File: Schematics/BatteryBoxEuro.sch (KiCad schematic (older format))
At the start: 16 parts, among them K1 JD2912-1Z-12VDC_40A, P1 Conn_WallPlug, U1 Terminal16, U2 F_Distributor, U3 NAC3MPA-1-WOT, U4 DPlusSimulator, U5 Pulser, U6 230V_KfzCharger, X1 X3, X2 12VKfz_Plug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

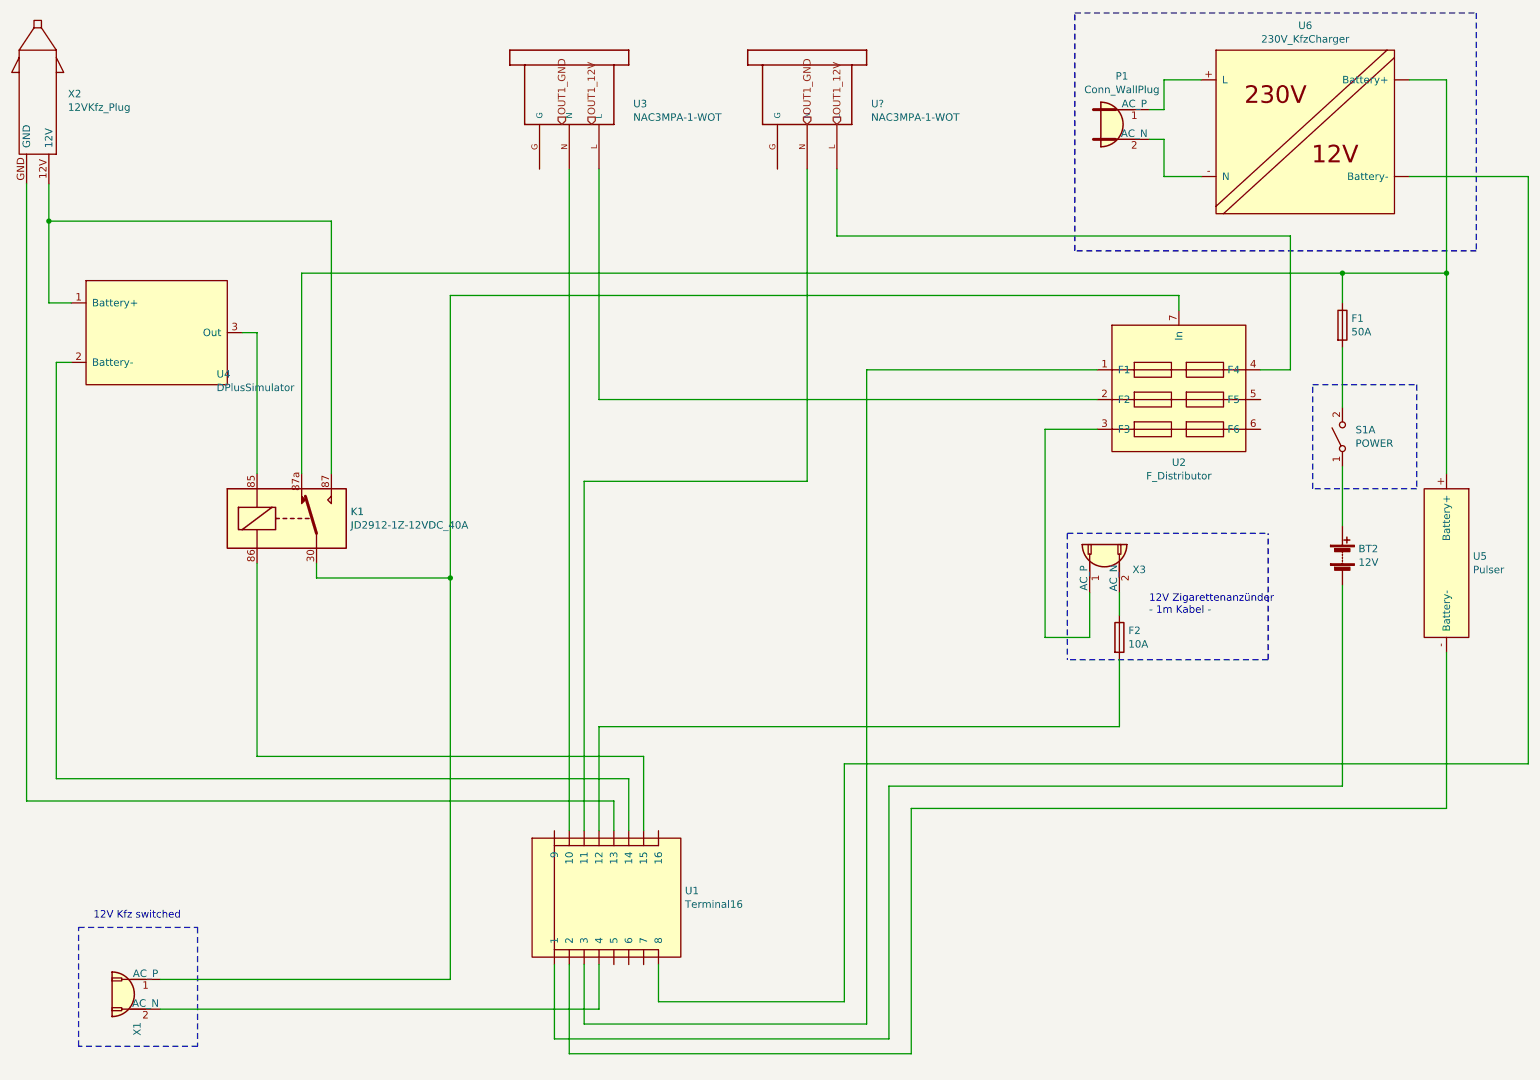
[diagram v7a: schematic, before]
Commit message: optimize layout
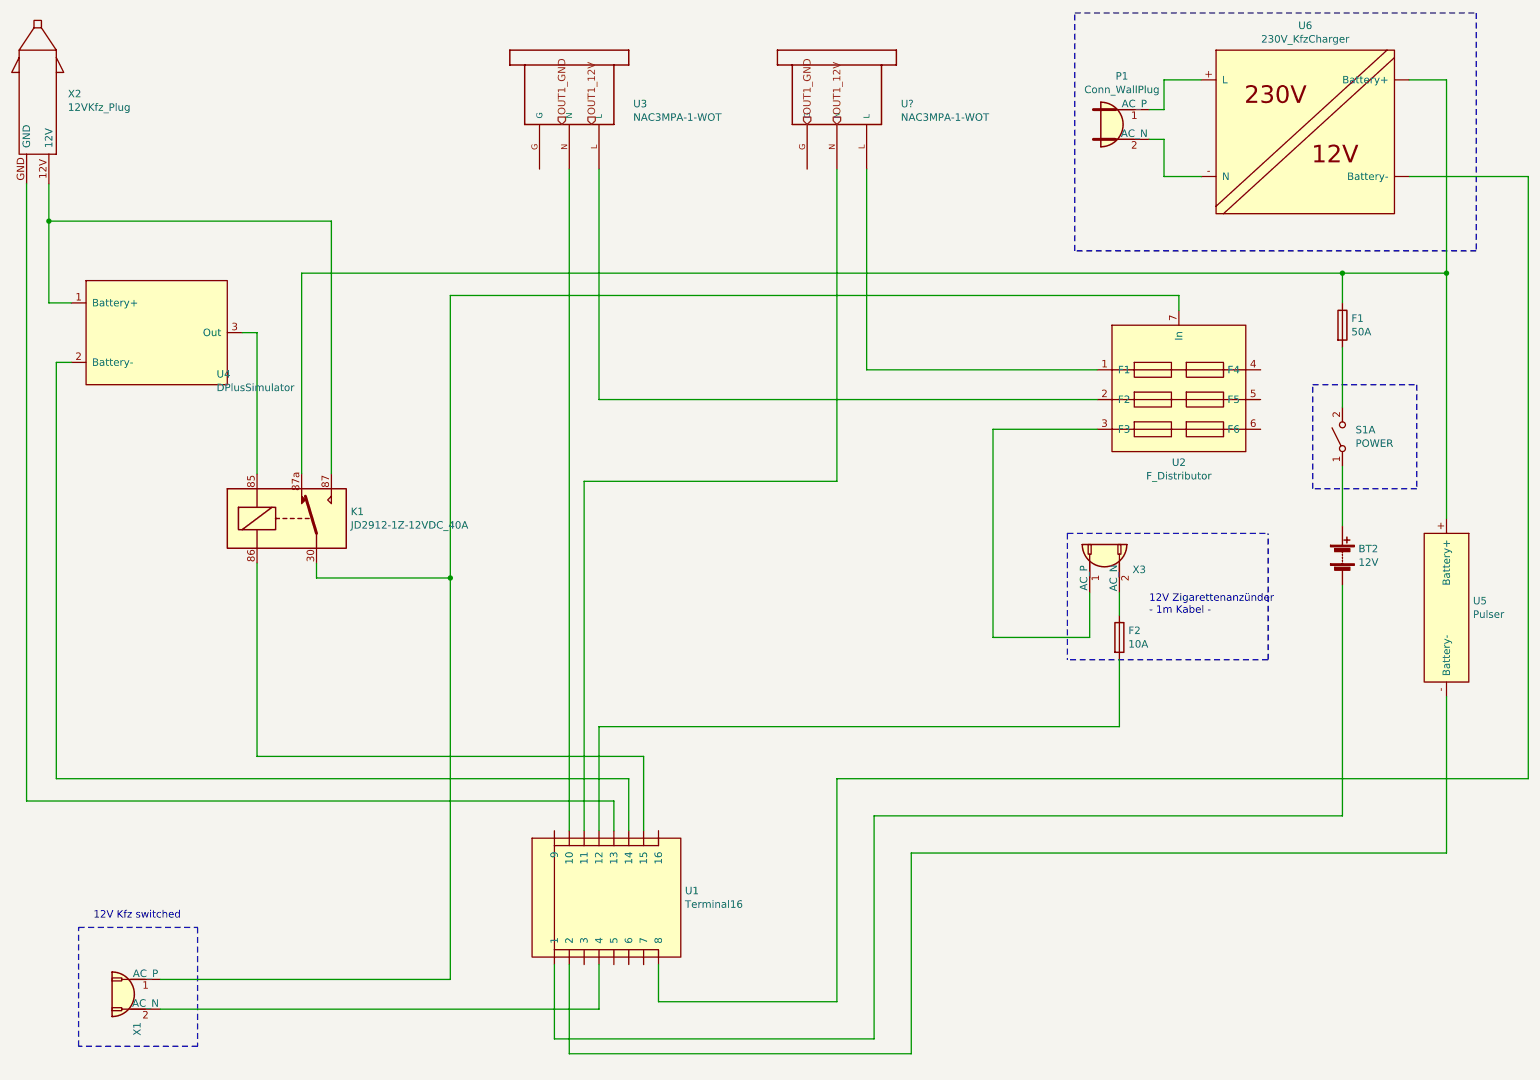
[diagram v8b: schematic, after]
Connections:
- net at U2.1 (F1): now also U?.L; no longer U1.~ (9)
- net at U2.4 (F4): no longer U?.L
- net at U1.~ (9): now also U?.N
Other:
- moved on the sheet: U5, U?
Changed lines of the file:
@@
 L MyParts:Pulser U5
 U 1 1 5E879508
-P 10400 4300
-F 0 "U5" V 10354 4378 50  0000 L CNN
-F 1 "Pulser" V 10445 4378 50  0000 L CNN
-F 2 "" H 10400 4300 50  0001 C CNN
-F 3 "" H 10400 4300 50  0001 C CNN
-	1    10400 4300
+P 10400 4600
+F 0 "U5" V 10354 4678 50  0000 L CNN
+F 1 "Pulser" V 10445 4678 50  0000 L CNN
+F 2 "" H 10400 4600 50  0001 C CNN
+F 3 "" H 10400 4600 50  0001 C CNN
+	1    10400 4600
 	0    1    1    0
 $EndComp
@@
 $EndComp
 Wire Wire Line
-	4300 7500 6550 7500
-Wire Wire Line
-	6550 7500 6550 5800
-Wire Wire Line
-	6550 5800 9600 5800
+	4300 7500 6450 7500
+Wire Wire Line
+	6450 7500 6450 6000
+Wire Wire Line
+	6450 6000 9600 6000
 Wire Wire Line
 	4800 6100 4800 5750
@@
 	4400 7600 6700 7600
 Wire Wire Line
-	6700 7600 6700 5950
-Wire Wire Line
-	6700 5950 10300 5950
-Wire Wire Line
-	10300 4900 10300 5950
-Wire Wire Line
-	4500 7400 6400 7400
-Wire Wire Line
-	4500 7000 4500 7400
+	6700 7600 6700 6250
+Wire Wire Line
+	6700 6250 10300 6250
+Wire Wire Line
+	10300 5200 10300 6250
 $Comp
 L Connector:Conn_WallSocket X3
@@
 	7900 4500 7900 4800
 Wire Wire Line
-	7900 4800 7600 4800
-Wire Wire Line
-	7600 4800 7600 3400
+	7900 4800 7250 4800
+Wire Wire Line
+	7250 4800 7250 3400
 Wire Notes Line
 	9100 4950 7750 4950
@@
 	9400 3800 9400 3100
 Wire Wire Line
-	7600 3400 7950 3400
+	7250 3400 7950 3400
 Wire Wire Line
 	4600 5400 8100 5400
@@
 $EndComp
 Wire Wire Line
-	9600 4450 9600 5800
+	9600 4450 9600 6000
 Wire Wire Line
 	9600 4050 9600 3650
@@
 	9600 2350 10300 2350
 Wire Wire Line
-	10300 2350 10300 3700
+	10300 2350 10300 4000
 Wire Wire Line
 	10050 1050 10300 1050
@@
 	5000 7000 5000 7250
 Wire Wire Line
-	5000 7250 6250 7250
-Wire Wire Line
-	6250 7250 6250 5650
-Wire Wire Line
-	6250 5650 10850 5650
-Wire Wire Line
-	10850 5650 10850 1700
+	5000 7250 6200 7250
+Wire Wire Line
+	6200 7250 6200 5750
+Wire Wire Line
+	6200 5750 10850 5750
+Wire Wire Line
+	10850 5750 10850 1700
 Wire Wire Line
 	10850 1700 10050 1700
@@
 	6400 3000 7950 3000
 Wire Wire Line
-	6400 3000 6400 7400
-Wire Wire Line
 	4400 1650 4400 6100
 $Comp
 L NAC3MPA-1-WOT:NAC3MPA-1-WOT U?
 U 1 1 5F024C85
-P 5800 1450
-F 0 "U?" V 5561 2080 50  0000 L CNN
-F 1 "NAC3MPA-1-WOT" V 5652 2080 50  0000 L CNN
-F 2 "NAC3MPA-1-WOT" H 5800 1450 50  0001 L BNN
-F 3 "" H 5800 1450 50  0001 C CNN
-	1    5800 1450
+P 6000 1450
+F 0 "U?" V 5761 2080 50  0000 L CNN
+F 1 "NAC3MPA-1-WOT" V 5852 2080 50  0000 L CNN
+F 2 "NAC3MPA-1-WOT" H 6000 1450 50  0001 L BNN
+F 3 "" H 6000 1450 50  0001 C CNN
+	1    6000 1450
 	0    1    1    0
 $EndComp
@@
 	4500 6100 4500 3750
 Wire Wire Line
-	4500 3750 6000 3750
-Wire Wire Line
-	6000 3750 6000 1650
-Wire Wire Line
-	9050 3000 9250 3000
-Wire Wire Line
-	9250 3000 9250 2100
-Wire Wire Line
-	9250 2100 6200 2100
-Wire Wire Line
-	6200 2100 6200 1650
+	4500 3750 6200 3750
 Text HLabel 6000 1350 1    50   Input ~ 0
 OUT1_GND
 Text HLabel 6200 1350 1    50   Input ~ 0
 OUT1_12V
+Wire Wire Line
+	6200 3750 6200 1650
+Wire Wire Line
+	6400 1650 6400 3000
 $EndSCHEMATC
